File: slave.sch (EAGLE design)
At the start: 12 parts

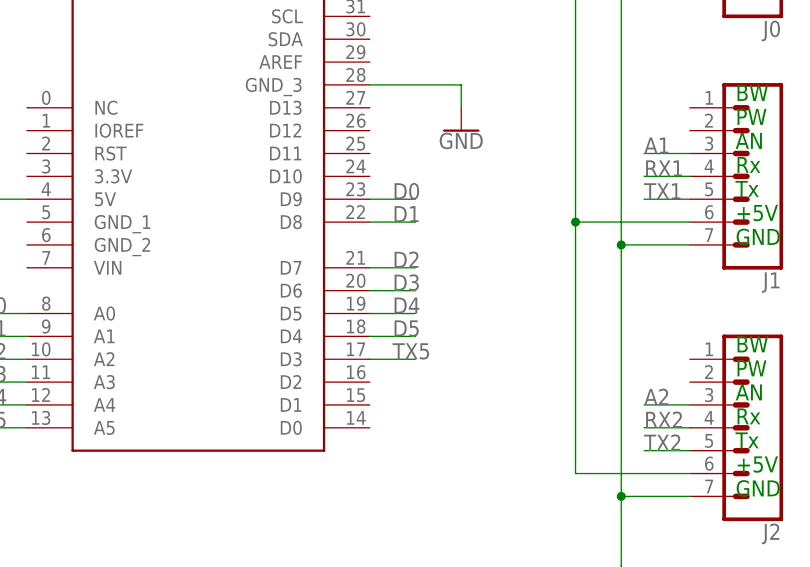
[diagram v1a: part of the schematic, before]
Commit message: update for CAN Bus shield
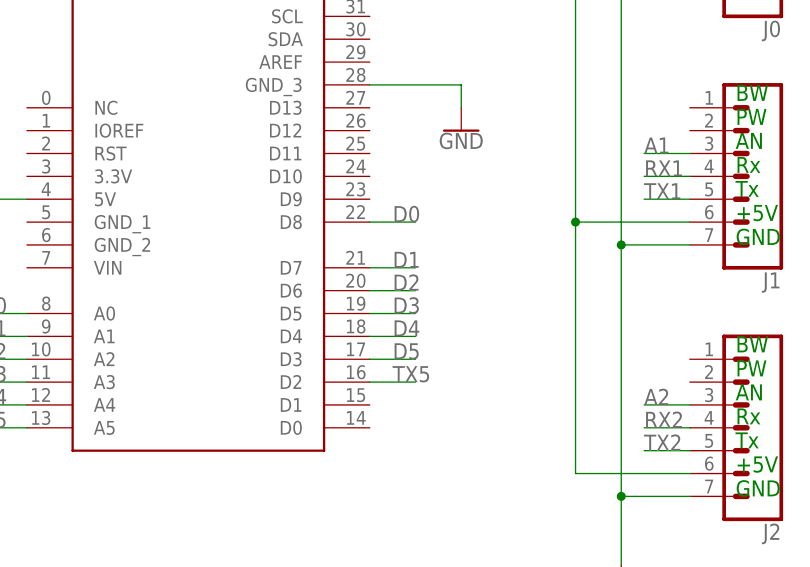
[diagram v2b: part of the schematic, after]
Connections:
- net D0: now also U$1.D8; no longer U$1.D9
- net D1: now also U$1.D7; no longer U$1.D8
- net D2: now also U$1.D6; no longer U$1.D7
- net D3: now also U$1.D5; no longer U$1.D6
- net D4: now also U$1.D4; no longer U$1.D5
- net D5: now also U$1.D3; no longer U$1.D4
- net TX5: now also U$1.D2; no longer U$1.D3
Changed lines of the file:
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@@
 </segment>
 <segment>
-<pinref part="U$1" gate="G$1" pin="D4"/>
-<wire x1="83.82" y1="78.74" x2="88.9" y2="78.74" width="0.1524" layer="91"/>
-<label x="86.36" y="78.74" size="1.778" layer="95"/>
+<pinref part="U$1" gate="G$1" pin="D3"/>
+<wire x1="83.82" y1="76.2" x2="88.9" y2="76.2" width="0.1524" layer="91"/>
+<label x="86.36" y="76.2" size="1.778" layer="95"/>
 </segment>
 </net>
@@
 </segment>
 <segment>
-<pinref part="U$1" gate="G$1" pin="D5"/>
-<wire x1="83.82" y1="81.28" x2="88.9" y2="81.28" width="0.1524" layer="91"/>
-<label x="86.36" y="81.28" size="1.778" layer="95"/>
+<pinref part="U$1" gate="G$1" pin="D4"/>
+<wire x1="83.82" y1="78.74" x2="88.9" y2="78.74" width="0.1524" layer="91"/>
+<label x="86.36" y="78.74" size="1.778" layer="95"/>
 </segment>
 </net>
@@
 </segment>
 <segment>
-<pinref part="U$1" gate="G$1" pin="D6"/>
-<wire x1="83.82" y1="83.82" x2="88.9" y2="83.82" width="0.1524" layer="91"/>
-<label x="86.36" y="83.82" size="1.778" layer="95"/>
+<pinref part="U$1" gate="G$1" pin="D5"/>
+<wire x1="83.82" y1="81.28" x2="88.9" y2="81.28" width="0.1524" layer="91"/>
+<label x="86.36" y="81.28" size="1.778" layer="95"/>
 </segment>
 </net>
@@
 </segment>
 <segment>
-<pinref part="U$1" gate="G$1" pin="D7"/>
-<wire x1="83.82" y1="86.36" x2="88.9" y2="86.36" width="0.1524" layer="91"/>
-<label x="86.36" y="86.36" size="1.778" layer="95"/>
+<pinref part="U$1" gate="G$1" pin="D6"/>
+<wire x1="83.82" y1="83.82" x2="88.9" y2="83.82" width="0.1524" layer="91"/>
+<label x="86.36" y="83.82" size="1.778" layer="95"/>
 </segment>
 </net>
@@
 </segment>
 <segment>
-<pinref part="U$1" gate="G$1" pin="D8"/>
-<wire x1="83.82" y1="91.44" x2="88.9" y2="91.44" width="0.1524" layer="91"/>
-<label x="86.36" y="91.44" size="1.778" layer="95"/>
+<pinref part="U$1" gate="G$1" pin="D7"/>
+<wire x1="83.82" y1="86.36" x2="88.9" y2="86.36" width="0.1524" layer="91"/>
+<label x="86.36" y="86.36" size="1.778" layer="95"/>
 </segment>
 </net>
@@
 </segment>
 <segment>
-<pinref part="U$1" gate="G$1" pin="D9"/>
-<wire x1="83.82" y1="93.98" x2="88.9" y2="93.98" width="0.1524" layer="91"/>
-<label x="86.36" y="93.98" size="1.778" layer="95"/>
+<pinref part="U$1" gate="G$1" pin="D8"/>
+<wire x1="83.82" y1="91.44" x2="88.9" y2="91.44" width="0.1524" layer="91"/>
+<label x="86.36" y="91.44" size="1.778" layer="95"/>
 </segment>
 </net>
@@
 </segment>
 <segment>
-<pinref part="U$1" gate="G$1" pin="D3"/>
-<wire x1="83.82" y1="76.2" x2="88.9" y2="76.2" width="0.1524" layer="91"/>
-<label x="86.36" y="76.2" size="1.778" layer="95"/>
+<pinref part="U$1" gate="G$1" pin="D2"/>
+<wire x1="83.82" y1="73.66" x2="88.9" y2="73.66" width="0.1524" layer="91"/>
+<label x="86.36" y="73.66" size="1.778" layer="95"/>
 </segment>
 </net>
